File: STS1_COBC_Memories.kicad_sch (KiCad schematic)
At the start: 6 parts, among them U1 W25Q01JVZEIQ, U17 CY15B108QN-40SXI

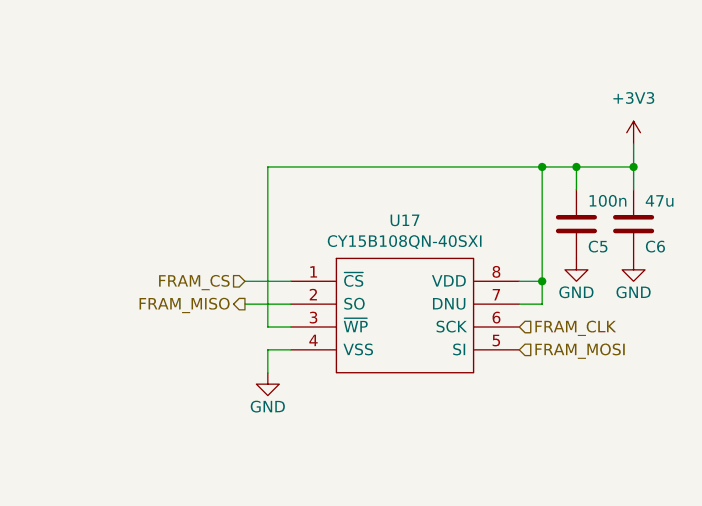
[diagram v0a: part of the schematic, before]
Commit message: Change FRAM to the one recommended by Infineon: CY15B108QN-40SXI -> CY15B104Q-SXI
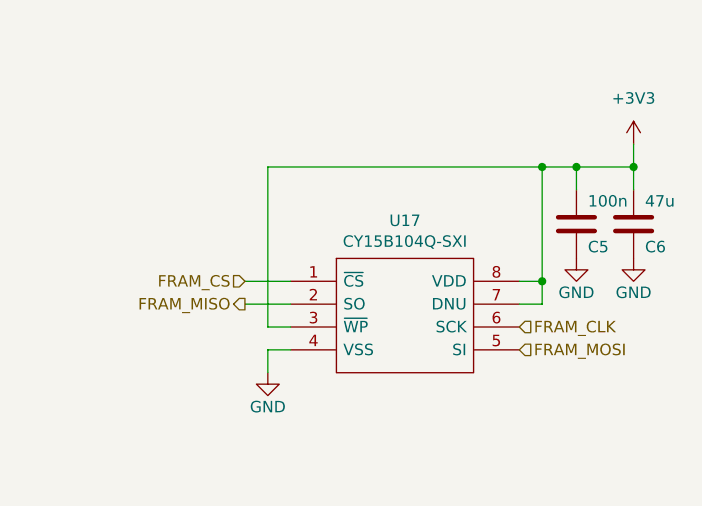
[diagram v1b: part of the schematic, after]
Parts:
- U17: value CY15B108QN-40SXI -> CY15B104Q-SXI; Arrow Part Number CY15B108QN-40SXI -> (none); Arrow Price/Stock https://www.arrow.com/en/products/cy15b108qn-40sxi/cypress-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 -> (none); Height 2.03 -> (none); Manufacturer_Name Cypress Semiconductor -> Infineon; Manufacturer_Part_Number CY15B108QN-40SXI -> CY15B104Q-SXI; Mouser Part Number 727-CY15B108QN-40SXI -> 727-CY15B104Q-SXI; Mouser Price/Stock https://www.mouser.co.uk/ProductDetail/Cypress-Semiconducto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 -> (none)
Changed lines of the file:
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@@
     (in_bom yes) (on_board yes)
     (property "Reference" "U17" (id 0) (at 209.55 66.929 0))
-    (property "Value" "CY15B108QN-40SXI" (id 1) (at 209.55 69.2404 0))
+    (property "Value" "CY15B104Q-SXI" (id 1) (at 209.55 69.2404 0))
     (property "Footprint" "STSLib:SOIC127P800X203-8N" (id 2) (at 218.44 71.12 0)
       (effects (font (size 1.27 1.27)) (justify left) hide)
     )
-    (property "Datasheet" "https://www.cypress.com/file/444186/download" (id 3) (at 218.44 73.66 0)
+    (property "Datasheet" "https://www.infineon.com/dgdl/Infineon-CY15B104Q_4-Mbit_(512_K_8)_Serial_(SPI)_F-RAM-DataSheet-v06_00-EN.pdf?fileId=8ac78c8c7d0d8da4017d0ecdc6684848" (id 3) (at 218.44 73.66 0)
       (effects (font (size 1.27 1.27)) (justify left) hide)
     )
@@
       (effects (font (size 1.27 1.27)) (justify left) hide)
     )
-    (property "Height" "2.03" (id 5) (at 218.44 78.74 0)
+    (property "Height" "" (id 5) (at 218.44 78.74 0)
       (effects (font (size 1.27 1.27)) (justify left) hide)
     )
-    (property "Manufacturer_Name" "Cypress Semiconductor" (id 6) (at 218.44 81.28 0)
+    (property "Manufacturer_Name" "Infineon" (id 6) (at 218.44 81.28 0)
       (effects (font (size 1.27 1.27)) (justify left) hide)
     )
-    (property "Manufacturer_Part_Number" "CY15B108QN-40SXI" (id 7) (at 218.44 83.82 0)
+    (property "Manufacturer_Part_Number" "CY15B104Q-SXI" (id 7) (at 218.44 83.82 0)
       (effects (font (size 1.27 1.27)) (justify left) hide)
     )
-    (property "Mouser Part Number" "727-CY15B108QN-40SXI" (id 8) (at 218.44 86.36 0)
+    (property "Mouser Part Number" "727-CY15B104Q-SXI " (id 8) (at 218.44 86.36 0)
       (effects (font (size 1.27 1.27)) (justify left) hide)
     )
-    (property "Mouser Price/Stock" "https://www.mouser.co.uk/ProductDetail/Cypress-Semiconductor/CY15B108QN-40SXI?qs=P1JMDcb91o4DSS%2FkAQM5uA%3D%3D" (id 9) (at 218.44 88.9 0)
+    (property "Mouser Price/Stock" "" (id 9) (at 218.44 88.9 0)
       (effects (font (size 1.27 1.27)) (justify left) hide)
     )
-    (property "Arrow Part Number" "CY15B108QN-40SXI" (id 10) (at 218.44 91.44 0)
+    (property "Arrow Part Number" "" (id 10) (at 218.44 91.44 0)
       (effects (font (size 1.27 1.27)) (justify left) hide)
     )
-    (property "Arrow Price/Stock" "https://www.arrow.com/en/products/cy15b108qn-40sxi/cypress-semiconductor?region=nac" (id 11) (at 218.44 93.98 0)
+    (property "Arrow Price/Stock" "" (id 11) (at 218.44 93.98 0)
       (effects (font (size 1.27 1.27)) (justify left) hide)
     )

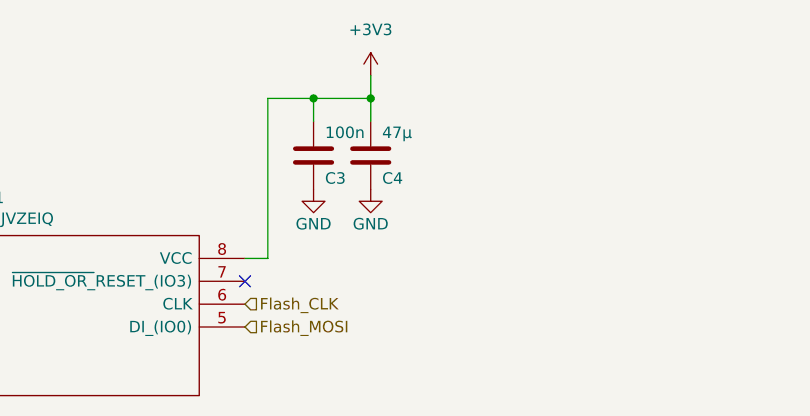
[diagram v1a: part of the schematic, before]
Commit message: Add manufacture number and JLCPCB part number to components
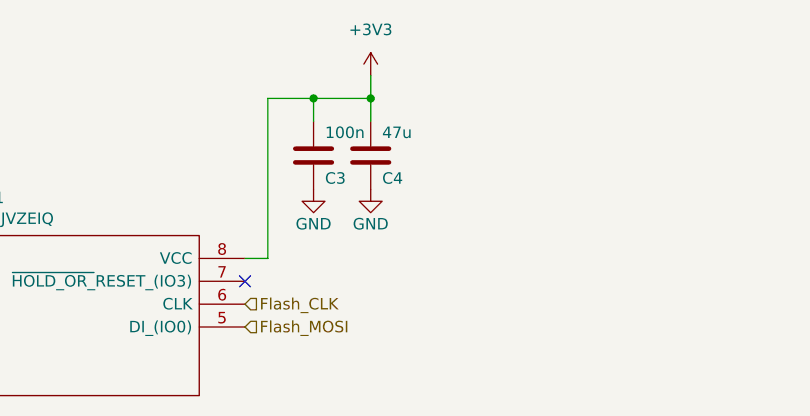
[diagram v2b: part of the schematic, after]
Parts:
- C3, C5: JLCPCB Part # (none) -> C1591; Manufacturer_Part_Number (none) -> CL10B104KB8NNNC
- C4: value 47µ -> 47u; JLCPCB Part # (none) -> C730416; Manufacturer_Part_Number (none) -> CL10A476MQ8QRNC
- C6: JLCPCB Part # (none) -> C730416; Manufacturer_Part_Number (none) -> CL10A476MQ8QRNC
- U1: JLCPCB Part # (none) -> C5137036
- U17: JLCPCB Part # (none) -> C2759922
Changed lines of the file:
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@@
       (effects (font (size 1.27 1.27)) (justify left) hide)
+    )
+    (property "JLCPCB Part #" "C5137036" (id 13) (at 53.34 71.12 0)
+      (effects (font (size 1.27 1.27)) hide)
     )
     (pin "1")
@@
       (effects (font (size 1.27 1.27)) (justify left) hide)
     )
+    (property "JLCPCB Part #" "C2759922" (id 12) (at 196.85 73.66 0)
+      (effects (font (size 1.27 1.27)) hide)
+    )
     (pin "1")
     (pin "2")
@@
       (effects (font (size 1.27 1.27)) hide)
     )
+    (property "JLCPCB Part #" "C1591" (id 4) (at 116.84 59.69 0)
+      (effects (font (size 1.27 1.27)) hide)
+    )
+    (property "Manufacturer_Part_Number" "CL10B104KB8NNNC " (id 5) (at 116.84 59.69 0)
+      (effects (font (size 1.27 1.27)) hide)
+    )
     (pin "1")
     (pin "2")
@@
       (effects (font (size 1.27 1.27)) (justify right))
     )
-    (property "Value" "47µ" (id 1) (at 124.46 57.15 0)
+    (property "Value" "47u" (id 1) (at 124.46 57.15 0)
       (effects (font (size 1.27 1.27)) (justify right))
     )
@@
     )
     (property "Datasheet" "~" (id 3) (at 123.19 59.69 0)
+      (effects (font (size 1.27 1.27)) hide)
+    )
+    (property "JLCPCB Part #" "C730416" (id 4) (at 123.19 59.69 0)
+      (effects (font (size 1.27 1.27)) hide)
+    )
+    (property "Manufacturer_Part_Number" "CL10A476MQ8QRNC " (id 5) (at 123.19 59.69 0)
       (effects (font (size 1.27 1.27)) hide)
     )
@@
       (effects (font (size 1.27 1.27)) hide)
     )
+    (property "JLCPCB Part #" "C1591" (id 4) (at 228.6 67.31 0)
+      (effects (font (size 1.27 1.27)) hide)
+    )
+    (property "Manufacturer_Part_Number" "CL10B104KB8NNNC " (id 5) (at 228.6 67.31 0)
+      (effects (font (size 1.27 1.27)) hide)
+    )
     (pin "1")
     (pin "2")
@@
       (effects (font (size 1.27 1.27)) hide)
     )
+    (property "JLCPCB Part #" "C730416" (id 4) (at 234.95 67.31 0)
+      (effects (font (size 1.27 1.27)) hide)
+    )
+    (property "Manufacturer_Part_Number" "CL10A476MQ8QRNC " (id 5) (at 234.95 67.31 0)
+      (effects (font (size 1.27 1.27)) hide)
+    )

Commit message: Update the manufacturer part number for some of components to be compatible with avaiable parts in the JLC parts database
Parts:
- C3, C5: JLCPCB Part # C1591 -> C129621; Manufacturer_Part_Number CL10B104KB8NNNC -> C0603C104K5RACAUTO
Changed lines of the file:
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@@
       (effects (font (size 1.27 1.27)) hide)
     )
-    (property "JLCPCB Part #" "C1591" (id 4) (at 116.84 59.69 0)
+    (property "JLCPCB Part #" "C129621" (id 4) (at 116.84 59.69 0)
       (effects (font (size 1.27 1.27)) hide)
     )
-    (property "Manufacturer_Part_Number" "CL10B104KB8NNNC " (id 5) (at 116.84 59.69 0)
+    (property "Manufacturer_Part_Number" "C0603C104K5RACAUTO" (id 5) (at 116.84 59.69 0)
       (effects (font (size 1.27 1.27)) hide)
     )
@@
       (effects (font (size 1.27 1.27)) hide)
     )
-    (property "JLCPCB Part #" "C1591" (id 4) (at 228.6 67.31 0)
+    (property "JLCPCB Part #" "C129621" (id 4) (at 228.6 67.31 0)
       (effects (font (size 1.27 1.27)) hide)
     )
-    (property "Manufacturer_Part_Number" "CL10B104KB8NNNC " (id 5) (at 228.6 67.31 0)
+    (property "Manufacturer_Part_Number" "C0603C104K5RACAUTO" (id 5) (at 228.6 67.31 0)
       (effects (font (size 1.27 1.27)) hide)
     )
